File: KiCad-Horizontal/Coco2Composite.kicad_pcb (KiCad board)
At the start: 2 copper layers, 52 x 36.5 mm, 19 parts, among them J1 MA03-1, J2 MA05-1, J3 AUDIO_JACK_3.5MM_PTH, Q1 PN2907, Q2 2N2222, U1 MC1372

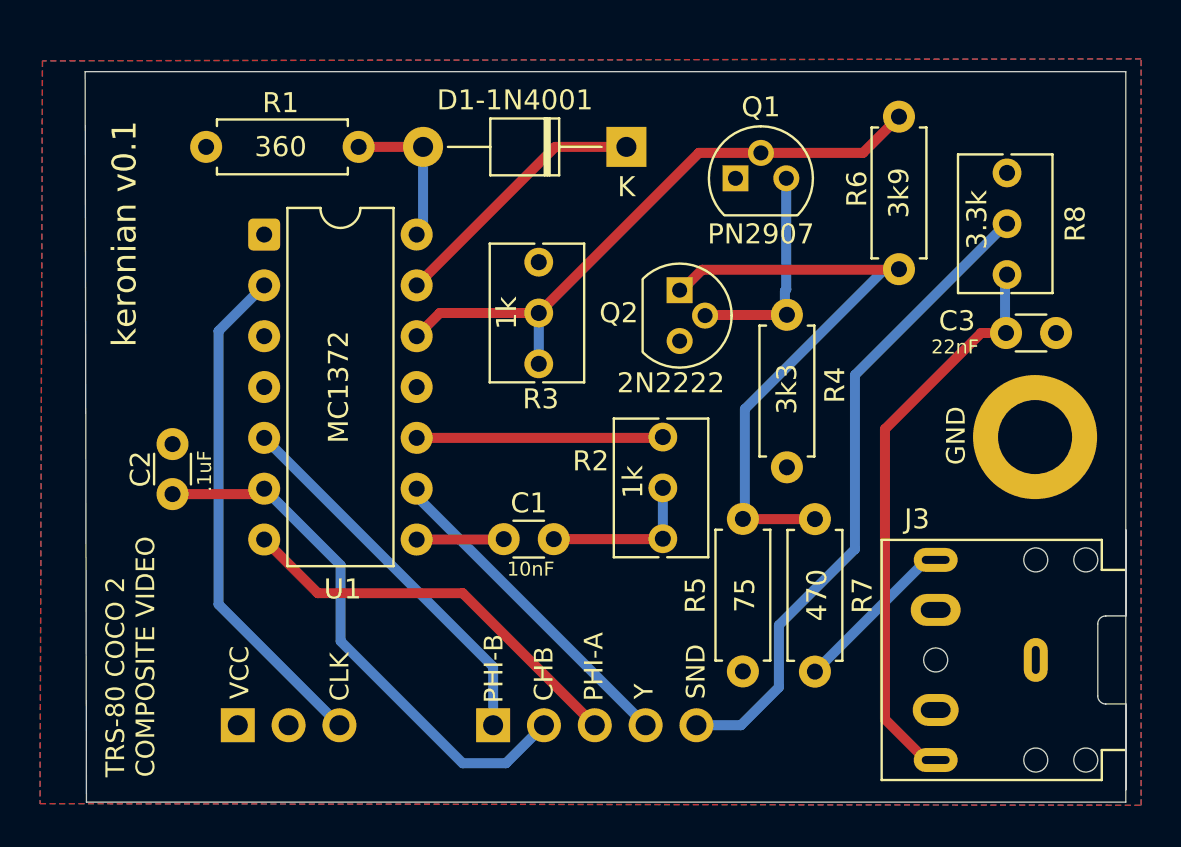
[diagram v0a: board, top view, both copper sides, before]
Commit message: Moved the audio jack over a little to make it a bit better centered
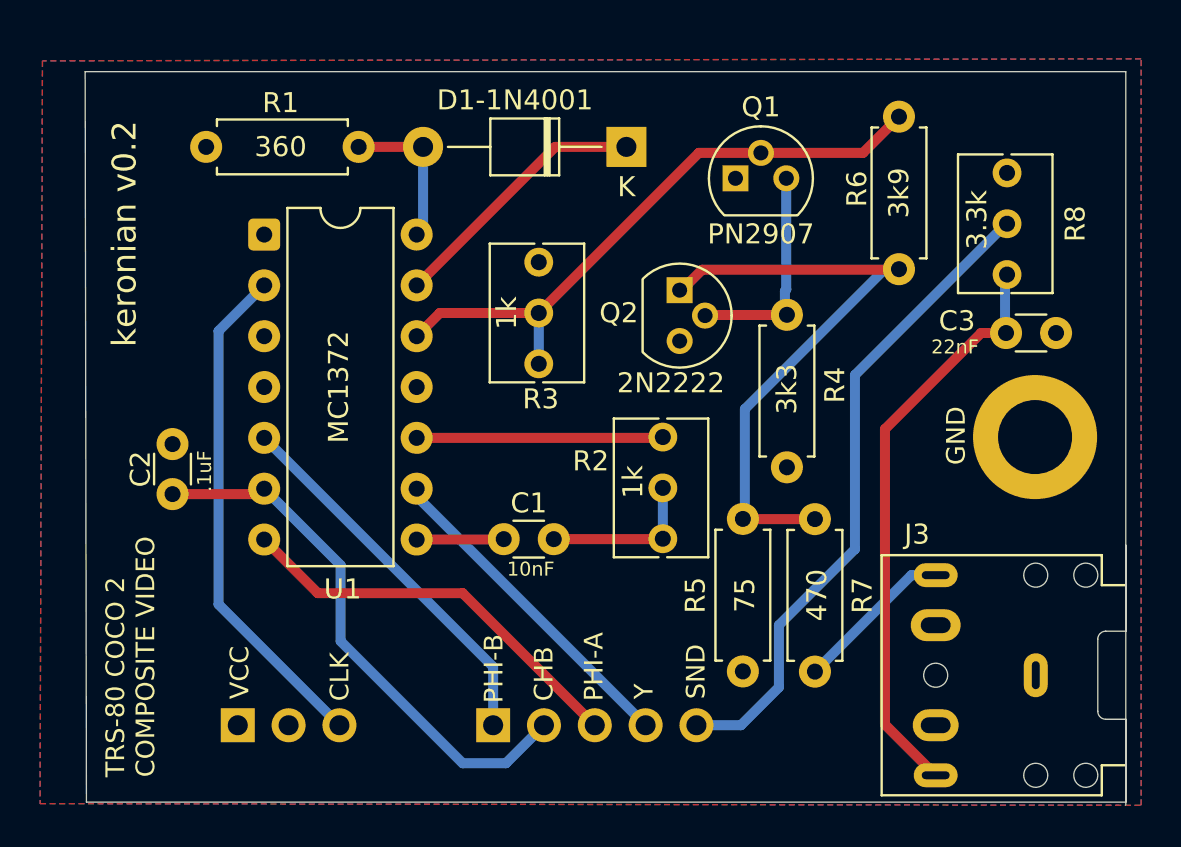
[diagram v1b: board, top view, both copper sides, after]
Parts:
- moved J3 0.76 mm to (163.5, 118.5)
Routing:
- net /SND_OUT: track 28.8 -> 29.4 mm
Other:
- board text added: "keronian v0.2"
- board text removed: "keronian v0.1"
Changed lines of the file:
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@@
 	(footprint "Connector_Audio:Jack_3.5mm_CUI_SJ1-3525N_Horizontal"
 		(layer "F.Cu")
-		(at 163.5342 117.737524 90)
+		(at 163.5342 118.5 90)
 		(descr "TRS 3.5mm, horizontal, through-hole, https://www.cuidevices.com/product/resource/pdf/sj1-352xn.pdf")
 		(tags "TRS audio jack stereo horizontal")
@@
 		)
 	)
-	(gr_text "keronian v0.1"
+	(gr_text "keronian v0.2"
 		(at 118.7 102.1 90)
 		(layer "F.SilkS")
@@
 	)
 	(segment
-		(start 158 122.7)
-		(end 156 120.7)
+		(start 158.5342 123.5)
+		(end 156 120.9658)
 		(width 0.5)
 		(layer "F.Cu")
@@
 	)
 	(segment
-		(start 156 120.7)
-		(end 156 106.2)
+		(start 160.8 101.4)
+		(end 162.05 101.4)
 		(width 0.5)
 		(layer "F.Cu")
@@
 	)
 	(segment
-		(start 158.5 122.7)
-		(end 158 122.7)
-		(width 0.5)
-		(layer "F.Cu")
-		(net 8)
-	)
-	(segment
-		(start 160.8 101.4)
-		(end 162.05 101.4)
+		(start 156 120.9658)
+		(end 156 106.2)
 		(width 0.5)
 		(layer "F.Cu")
@@
 	)
 	(segment
-		(start 158.12 112.7)
-		(end 152.5 118.32)
+		(start 158.5342 113.5)
+		(end 157.32 113.5)
 		(width 0.5)
 		(layer "B.Cu")
@@
 	)
 	(segment
-		(start 158.5 112.7)
-		(end 158.12 112.7)
+		(start 157.32 113.5)
+		(end 152.5 118.32)
 		(width 0.5)
 		(layer "B.Cu")

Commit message: Big changes to let the channel select switch disable color
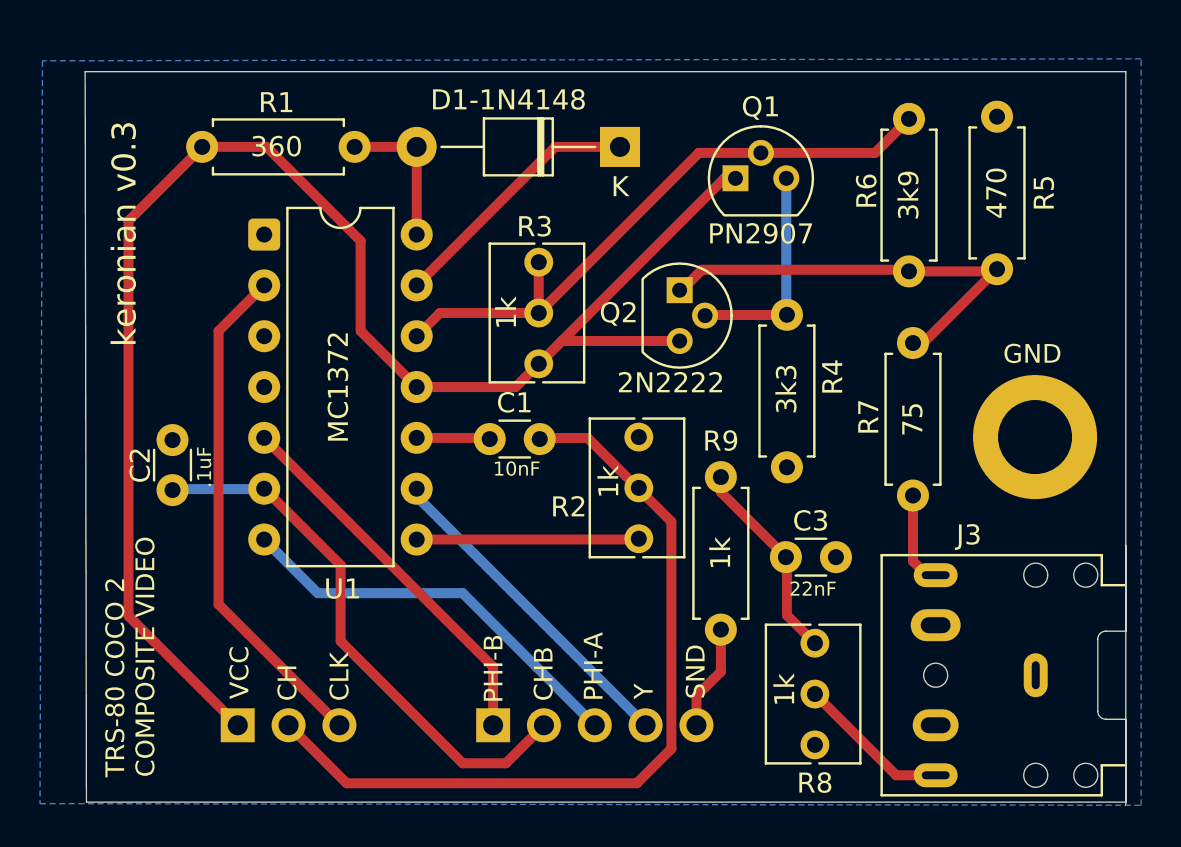
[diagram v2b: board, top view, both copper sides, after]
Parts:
- added R9: 1k, Resistor_THT:R_Axial_DIN0207_L6.3mm_D2.5mm_P7.62mm_Horizontal, F.Cu at (147.8, 108.6)
- D1-1N4148: renamed from D1-1N4001; value 1N4004 -> 1N4148
- R8: value 3.3k -> 1k
- moved R5 30.5 mm to (161.6, 90.6), turned to -90 degrees
- moved R8 25.4 mm to (152.5, 122.0)
- moved C3 15.7 mm to (151.1, 112.6)
- moved R7 10.1 mm to (157.4, 101.9)
- moved C1 5.05 mm to (136.2, 106.7)
- moved R2 1.20 mm to (143.7, 111.7)
- moved R6 0.51 mm to (157.2, 90.7)
- moved D1-1N4148 0.32 mm to (142.8, 92.1)
- moved C2 0.20 mm to (120.4, 109.2)
- moved R1 0.20 mm to (129.5, 92.1)
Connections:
- C1 pad 1: /CHROM_MOD_OUT -> /CHROM_IN
- C1 pad 2: /CHROM_BALANCE -> /CH
- C3 pad 1: /SND_OUT -> /SND_OUT_RES
- J1 pad 2: unconnected-(J1-Pad2) -> /CH
- R2 pad 1: /CHROM_BALANCE -> /CHROM_MOD_OUT
- R2 pad 2: /CHROM_BALANCE -> /CH
- R2 pad 3: /CHROM_IN -> GND
- R3 pad 1: /RF_OUT -> VCC
- R3 pad 3: VCC -> /RF_OUT
- R8 pad 1: /SND_OUT -> GND
- R8 pad 2: /SND -> /SND_OUT
- R8 pad 3: (no net) -> /SND_OUT_RES
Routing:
- net VCC: track 0.00 -> 77.2 mm
- net /CH: track 0.00 -> 40.6 mm
- net /SND: track 32.8 -> 5.29 mm
- net /SND_OUT: track 29.4 -> 7.72 mm
- net /SND_OUT_RES: track 0.00 -> 10.2 mm
- net /Q2_E: track 31.2 -> 22.1 mm
- net /CHROM_IN: track 12.3 -> 3.67 mm
- net /CHROM_BALANCE: track 8.00 -> 0.00 mm
- net /CHROM_MOD_OUT: track 4.36 -> 11.2 mm
- net /COMP_OUT: track 8.03 -> 4.70 mm
- added copper zone on B.Cu, net GND
- removed copper zone on F.Cu, net GND
- removed copper zone on B.Cu, net VCC
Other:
- board text added: "CH"
- board text added: "keronian v0.3"
- board text removed: "keronian v0.2"

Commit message: increased the footprint of the variable resistors to match what I have in the BOM, added a dot for orientation, switched schematic symbols to something more standard
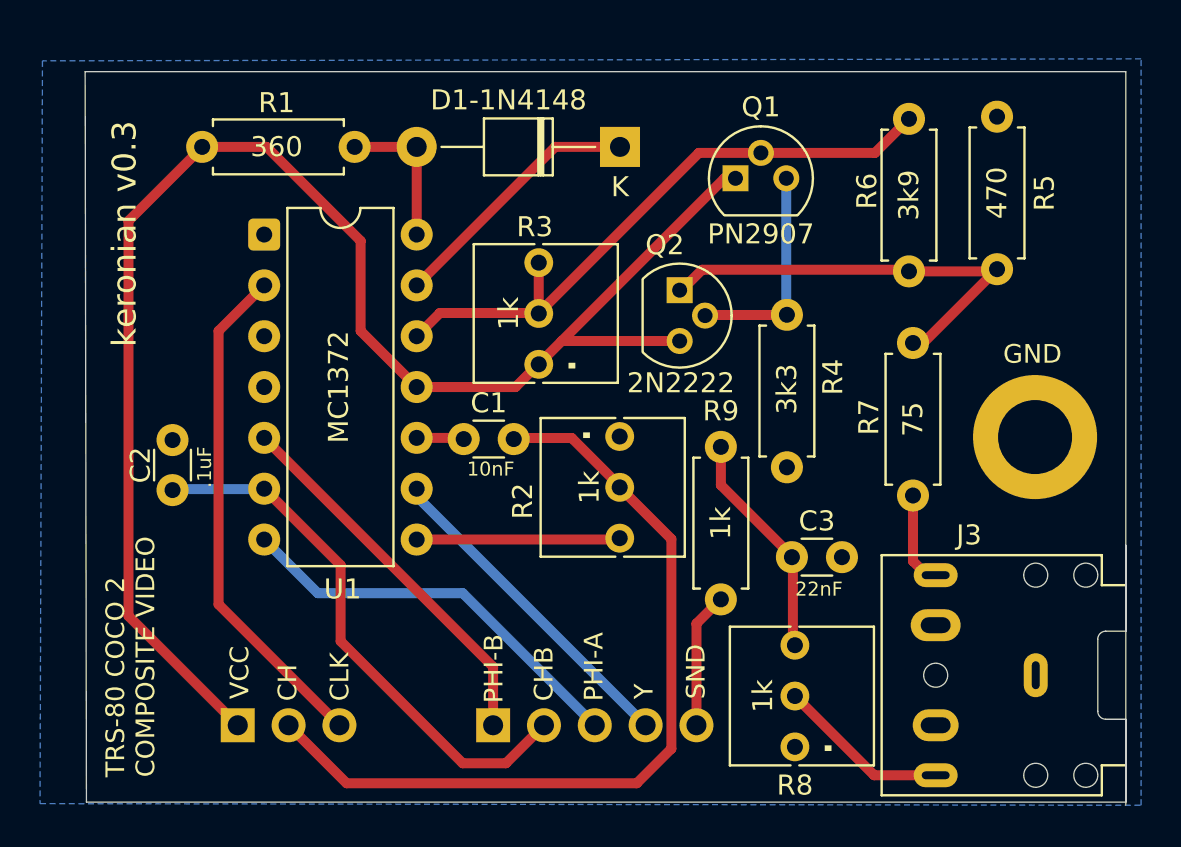
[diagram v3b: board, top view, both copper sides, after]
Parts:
- R2, R3, R8: footprint Potentiometer_THT:Potentiometer_Bourns_3266Y_Vertical -> Modified:Potentiometer_Bourns_3266Y_Vertical
- moved R2 5.20 mm to (142.7, 106.6), turned to 90 degrees
- moved R9 1.51 mm to (147.8, 107.1)
- moved C1 1.30 mm to (134.9, 106.7)
- moved R8 1.00 mm to (151.5, 122.1)
- moved C3 0.30 mm to (151.3, 112.6)
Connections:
- R2 pad 1: /CHROM_MOD_OUT -> GND
- R2 pad 3: GND -> /CHROM_MOD_OUT
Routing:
- net /SND: track 5.29 -> 6.80 mm
- net /CHROM_IN: track 3.67 -> 2.37 mm
- net /SND_OUT_RES: track 10.2 -> 11.3 mm
- net /CHROM_MOD_OUT: track 11.2 -> 10.2 mm
- net /CH: track 40.6 -> 41.6 mm
- net /SND_OUT: track 7.72 -> 8.67 mm

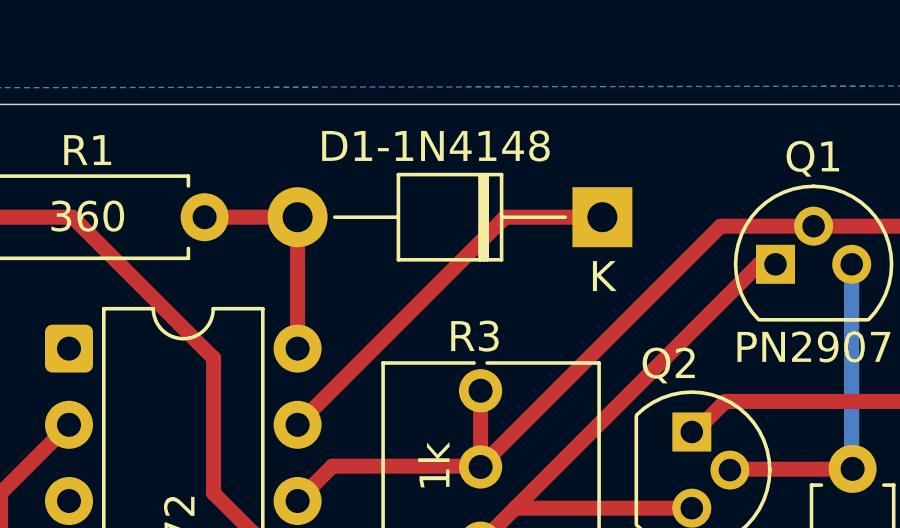
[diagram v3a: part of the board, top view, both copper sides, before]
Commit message: Changed diode footprint for smaller diode
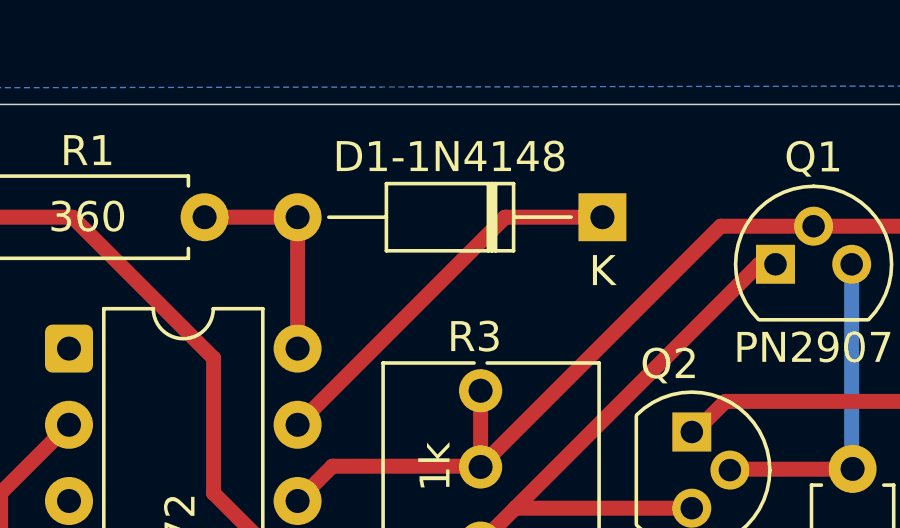
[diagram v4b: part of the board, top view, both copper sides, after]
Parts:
- D1-1N4148: footprint Diode_THT:D_T-1_P10.16mm_Horizontal -> Diode_THT:D_DO-35_SOD27_P10.16mm_Horizontal
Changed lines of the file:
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@@
 		)
 	)
-	(footprint "Diode_THT:D_T-1_P10.16mm_Horizontal"
+	(footprint "Diode_THT:D_DO-35_SOD27_P10.16mm_Horizontal"
 		(layer "F.Cu")
 		(at 142.76 92.1 180)
-		(descr "Diode, T-1 series, Axial, Horizontal, pin pitch=10.16mm, , length*diameter=3.2*2.6mm^2, , http://www.diodes.com/_files/packages/T-1.pdf")
-		(tags "Diode T-1 series Axial Horizontal pin pitch 10.16mm  length 3.2mm diameter 2.6mm")
+		(descr "Diode, DO-35_SOD27 series, Axial, Horizontal, pin pitch=10.16mm, , length*diameter=4*2mm^2, , http://www.diodes.com/_files/packages/DO-35.pdf")
+		(tags "Diode DO-35_SOD27 series Axial Horizontal pin pitch 10.16mm  length 4mm diameter 2mm")
 		(property "Reference" "D1-1N4148"
-			(at 5.569177 2.337664 0)
+			(at 5.08 2 180)
 			(layer "F.SilkS")
 			(effects
@@
 		)
 		(property "Value" "1N4148"
-			(at -2.430823 2.337664 0)
+			(at 5.08 2.12 180)
 			(layer "F.Fab")
 			(effects
@@
 		(attr through_hole)
 		(fp_line
-			(start 8.92 0)
-			(end 6.8 0)
-			(stroke
-				(width 0.12)
-				(type solid)
-			)
-			(layer "F.SilkS")
-		)
-		(fp_line
-			(start 6.8 1.42)
-			(end 6.8 -1.42)
-			(stroke
-				(width 0.12)
-				(type solid)
-			)
-			(layer "F.SilkS")
-		)
-		(fp_line
-			(start 6.8 -1.42)
-			(end 3.36 -1.42)
-			(stroke
-				(width 0.12)
-				(type solid)
-			)
-			(layer "F.SilkS")
-		)
-		(fp_line
-			(start 4.08 -1.42)
-			(end 4.08 1.42)
-			(stroke
-				(width 0.12)
-				(type solid)
-			)
-			(layer "F.SilkS")
-		)
-		(fp_line
-			(start 3.96 -1.42)
-			(end 3.96 1.42)
-			(stroke
-				(width 0.12)
-				(type solid)
-			)
-			(layer "F.SilkS")
-		)
-		(fp_line
-			(start 3.84 -1.42)
-			(end 3.84 1.42)
-			(stroke
-				(width 0.12)
-				(type solid)
-			)
-			(layer "F.SilkS")
-		)
-		(fp_line
-			(start 3.36 1.42)
-			(end 6.8 1.42)
-			(stroke
-				(width 0.12)
-				(type solid)
-			)
-			(layer "F.SilkS")
-		)
-		(fp_line
-			(start 3.36 -1.42)
-			(end 3.36 1.42)
-			(stroke
-				(width 0.12)
-				(type solid)
-			)
-			(layer "F.SilkS")
-		)
-		(fp_line
-			(start 1.24 0)
-			(end 3.36 0)
-			(stroke
-				(width 0.12)
-				(type solid)
-			)
-			(layer "F.SilkS")
-		)
-		(fp_line
-			(start 11.41 1.55)
-			(end 11.41 -1.55)
+			(start 9.12 0)
+			(end 7.2 0)
+			(stroke
+				(width 0.12)
+				(type solid)
+			)
+			(layer "F.SilkS")
+		)
+		(fp_line
+			(start 7.2 1.12)
+			(end 7.2 -1.12)
+			(stroke
+				(width 0.12)
+				(type solid)
+			)
+			(layer "F.SilkS")
+		)
+		(fp_line
+			(start 7.2 -1.12)
+			(end 2.96 -1.12)
+			(stroke
+				(width 0.12)
+				(type solid)
+			)
+			(layer "F.SilkS")
+		)
+		(fp_line
+			(start 3.8 -1.12)
+			(end 3.8 1.12)
+			(stroke
+				(width 0.12)
+				(type solid)
+			)
+			(layer "F.SilkS")
+		)
+		(fp_line
+			(start 3.68 -1.12)
+			(end 3.68 1.12)
+			(stroke
+				(width 0.12)
+				(type solid)
+			)
+			(layer "F.SilkS")
+		)
+		(fp_line
+			(start 3.56 -1.12)
+			(end 3.56 1.12)
+			(stroke
+				(width 0.12)
+				(type solid)
+			)
+			(layer "F.SilkS")
+		)
+		(fp_line
+			(start 2.96 1.12)
+			(end 7.2 1.12)
+			(stroke
+				(width 0.12)
+				(type solid)
+			)
+			(layer "F.SilkS")
+		)
+		(fp_line
+			(start 2.96 -1.12)
+			(end 2.96 1.12)
+			(stroke
+				(width 0.12)
+				(type solid)
+			)
+			(layer "F.SilkS")
+		)
+		(fp_line
+			(start 1.04 0)
+			(end 2.96 0)
+			(stroke
+				(width 0.12)
+				(type solid)
+			)
+			(layer "F.SilkS")
+		)
+		(fp_line
+			(start 11.21 1.25)
+			(end 11.21 -1.25)
 			(stroke
 				(width 0.05)
@@
 		)
 		(fp_line
-			(start 11.41 -1.55)
-			(end -1.25 -1.55)
+			(start 11.21 -1.25)
+			(end -1.05 -1.25)
 			(stroke
 				(width 0.05)
@@
 		)
 		(fp_line
-			(start -1.25 1.55)
-			(end 11.41 1.55)
+			(start -1.05 1.25)
+			(end 11.21 1.25)
 			(stroke
 				(width 0.05)
@@
 		)
 		(fp_line
-			(start -1.25 -1.55)
-			(end -1.25 1.55)
+			(start -1.05 -1.25)
+			(end -1.05 1.25)
 			(stroke
 				(width 0.05)
@@
 		(fp_line
 			(start 10.16 0)
-			(end 6.68 0)
-			(stroke
-				(width 0.1)
-				(type solid)
-			)
-			(layer "F.Fab")
-		)
-		(fp_line
-			(start 6.68 1.3)
-			(end 6.68 -1.3)
-			(stroke
-				(width 0.1)
-				(type solid)
-			)
-			(layer "F.Fab")
-		)
-		(fp_line
-			(start 6.68 -1.3)
-			(end 3.48 -1.3)
-			(stroke
-				(width 0.1)
-				(type solid)
-			)
-			(layer "F.Fab")
-		)
-		(fp_line
-			(start 4.06 -1.3)
-			(end 4.06 1.3)
-			(stroke
-				(width 0.1)
-				(type solid)
-			)
-			(layer "F.Fab")
-		)
-		(fp_line
-			(start 3.96 -1.3)
-			(end 3.96 1.3)
-			(stroke
-				(width 0.1)
-				(type solid)
-			)
-			(layer "F.Fab")
-		)
-		(fp_line
-			(start 3.86 -1.3)
-			(end 3.86 1.3)
-			(stroke
-				(width 0.1)
-				(type solid)
-			)
-			(layer "F.Fab")
-		)
-		(fp_line
-			(start 3.48 1.3)
-			(end 6.68 1.3)
-			(stroke
-				(width 0.1)
-				(type solid)
-			)
-			(layer "F.Fab")
-		)
-		(fp_line
-			(start 3.48 -1.3)
-			(end 3.48 1.3)
+			(end 7.08 0)
+			(stroke
+				(width 0.1)
+				(type solid)
+			)
+			(layer "F.Fab")
+		)
+		(fp_line
+			(start 7.08 1)
+			(end 7.08 -1)
+			(stroke
+				(width 0.1)
+				(type solid)
+			)
+			(layer "F.Fab")
+		)
+		(fp_line
+			(start 7.08 -1)
+			(end 3.08 -1)
+			(stroke
+				(width 0.1)
+				(type solid)
+			)
+			(layer "F.Fab")
+		)
+		(fp_line
+			(start 3.78 -1)
+			(end 3.78 1)
+			(stroke
+				(width 0.1)
+				(type solid)
+			)
+			(layer "F.Fab")
+		)
+		(fp_line
+			(start 3.68 -1)
+			(end 3.68 1)
+			(stroke
+				(width 0.1)
+				(type solid)
+			)
+			(layer "F.Fab")
+		)
+		(fp_line
+			(start 3.58 -1)
+			(end 3.58 1)
+			(stroke
+				(width 0.1)
+				(type solid)
+			)
+			(layer "F.Fab")
+		)
+		(fp_line
+			(start 3.08 1)
+			(end 7.08 1)
+			(stroke
+				(width 0.1)
+				(type solid)
+			)
+			(layer "F.Fab")
+		)
+		(fp_line
+			(start 3.08 -1)
+			(end 3.08 1)
 			(stroke
 				(width 0.1)
@@
 		(fp_line
 			(start 0 0)
-			(end 3.48 0)
+			(end 3.08 0)
 			(stroke
 				(width 0.1)
@@
 		)
 		(fp_text user "K"
-			(at 0 -2 0)
+			(at 0 -1.8 180)
 			(layer "F.SilkS")
 			(effects
@@
 		)
 		(fp_text user "K"
-			(at 0 -2 0)
+			(at 0 -1.8 180)
 			(layer "F.Fab")
 			(effects
@@
 		)
 		(fp_text user "${REFERENCE}"
-			(at 5.32 0 0)
-			(layer "F.Fab")
-			(effects
-				(font
-					(size 0.64 0.64)
-					(thickness 0.096)
+			(at 5.38 0 180)
+			(layer "F.Fab")
+			(effects
+				(font
+					(size 0.8 0.8)
+					(thickness 0.12)
 				)
 			)
@@
 		(pad "1" thru_hole rect
 			(at 0 0 180)
-			(size 2 2)
-			(drill 1)
+			(size 1.6 1.6)
+			(drill 0.8)
 			(layers "*.Cu" "*.Mask")
 			(remove_unused_layers no)
@@
 		(pad "2" thru_hole oval
 			(at 10.16 0 180)
-			(size 2 2)
-			(drill 1)
+			(size 1.6 1.6)
+			(drill 0.8)
 			(layers "*.Cu" "*.Mask")
 			(remove_unused_layers no)
@@
 		)
 		(embedded_fonts no)
-		(model "${KICAD9_3DMODEL_DIR}/Diode_THT.3dshapes/D_T-1_P10.16mm_Horizontal.wrl"
+		(model "${KICAD9_3DMODEL_DIR}/Diode_THT.3dshapes/D_DO-35_SOD27_P10.16mm_Horizontal.wrl"
 			(offset
 				(xyz 0 0 0)
